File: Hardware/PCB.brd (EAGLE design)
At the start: 46.2 x 35 mm, 105 parts, among them IC1 BQ25180YBGR_BQ25180YBGR, IC2 DRV2605YZFR, IC3 BMA421, IC9 RT6160AWSC, J1 503480-2400, J2 TC2030-IDC_TC2030-IDC, J4 KH-TYPE-C-16P, Q1 20V/4.2A/52mΩ/1.4W, Q3 SI1308EDL-T1-GE3, U1 NRF52840_QF, U3 MAX17048G+T10, X1 32MHz, X2 32.768kHz

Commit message: second commit
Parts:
- moved TP_GND 38.9 mm to (17.9, 97.3)
- moved TP_3.3V 31.8 mm to (21.6, 94.3)
- moved C27 27.9 mm to (19.8, 98.2)
- moved TP_VBAT 27.3 mm to (19.4, 95.3)
- moved D3 26.6 mm to (40.7, 97.4)
- moved TP_SCL 26.4 mm to (19.8, 87.3)
- moved L7 25.6 mm to (25.1, 94.3)
- moved TP_VREG 24.7 mm to (25.6, 91.3)
- moved TP_SWDIO 23.7 mm to (43.7, 93.4)
- moved U3 23.3 mm to (14.7, 97.8)
- moved C6 23.3 mm to (23.1, 77.5), turned to 180 degrees
- moved X2 22.2 mm to (16.8, 81.8)
- moved TP_SDA 22.2 mm to (19.7, 84.3)
- moved C29 22.0 mm to (33.1, 72.2)
- moved TP_SWDCLK 21.3 mm to (39.7, 90.2)
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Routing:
- net SDA/2.4C: track 117.4 -> 23.3 mm, vias 6 -> 4
- net DEC4_6: track 108.0 -> 24.9 mm, vias 10 -> 3
- net 3V3/2.4A: track 184.8 -> 119.8 mm, vias 10 -> 14
- net RESET: track 0.00 -> 34.8 mm, vias 0 -> 2
- net P0.13/1.5D: track 42.2 -> 8.18 mm
- net SCL/1.4C: track 7.60 -> 40.1 mm, vias 0 -> 2
- net SDA/1.4C: track 0.00 -> 31.7 mm, vias 0 -> 2
- net GND: track 399.6 -> 370.7 mm, vias 7 -> 12
- net SWDCLK: track 0.00 -> 26.9 mm, vias 0 -> 2
- net RESE: track 39.1 -> 12.3 mm, vias 5 -> 0
- net EPD_DC: track 0.00 -> 26.0 mm, vias 0 -> 2
- net N$10: track 21.1 -> 1.67 mm, vias 4 -> 0
- net N$13: track 0.00 -> 19.1 mm, vias 0 -> 2
- net N$15: track 9.46 -> 28.3 mm, vias 0 -> 2
- net N$17: track 23.5 -> 4.96 mm, vias 2 -> 0
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- added copper zone on layer 2, net GND

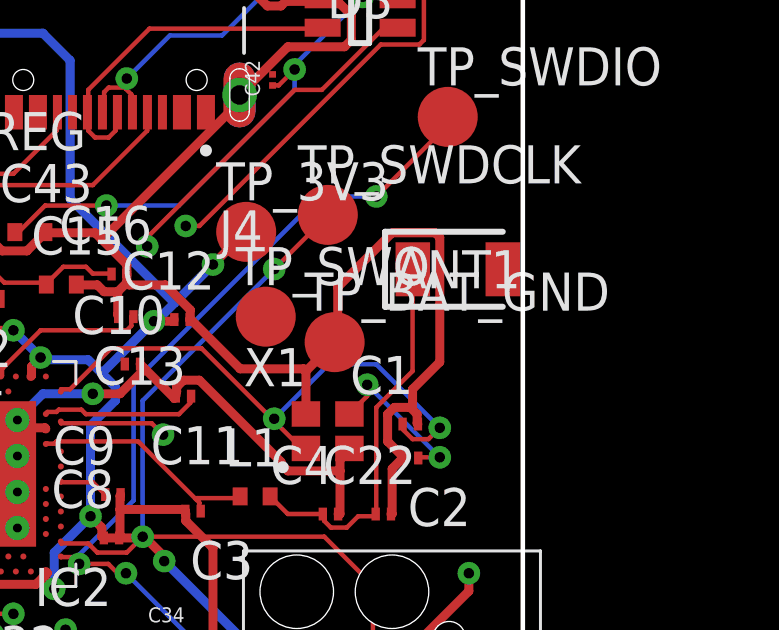
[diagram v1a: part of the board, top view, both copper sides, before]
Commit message: print out schematic
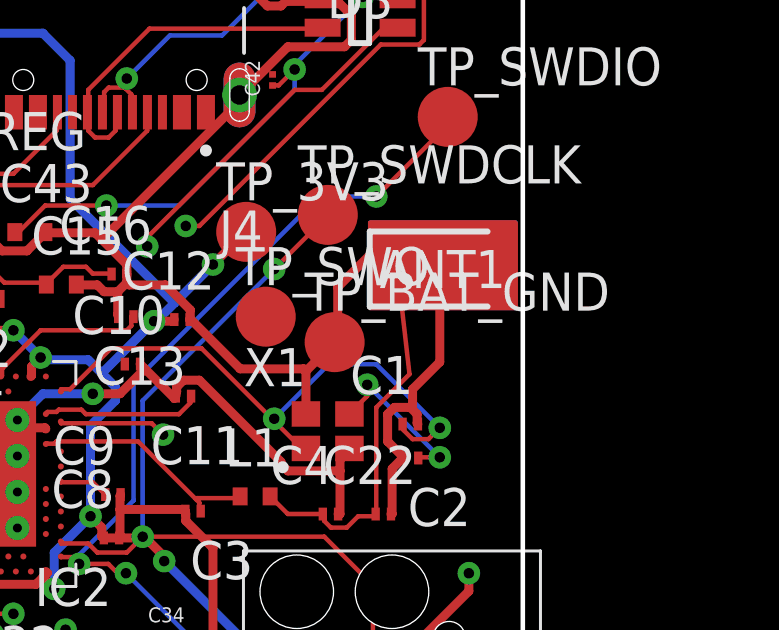
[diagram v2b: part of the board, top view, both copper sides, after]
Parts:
- moved ANT1 0.51 mm to (43.5, 88.4)
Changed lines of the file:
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@@
 <wire x1="38" y1="67" x2="38" y2="65" width="0.1524" layer="20"/>
 <wire x1="38" y1="65" x2="44.162278125" y2="65" width="0.1524" layer="20"/>
+<polygon width="0.1524" layer="2" pour="solid">
+<vertex x="41.0762" y="87.0762"/>
+<vertex x="45.9238" y="87.0762"/>
+<vertex x="45.9238" y="89.9238"/>
+<vertex x="41.0762" y="89.9238"/>
+</polygon>
+<polygon width="0.1524" layer="1" pour="solid">
+<vertex x="41.0762" y="87.0762"/>
+<vertex x="45.9238" y="87.0762"/>
+<vertex x="45.9238" y="89.9238"/>
+<vertex x="41.0762" y="89.9238"/>
+</polygon>
+<polygon width="0.1524" layer="15" pour="solid">
+<vertex x="41.0762" y="87.0762"/>
+<vertex x="45.9238" y="87.0762"/>
+<vertex x="45.9238" y="89.9238"/>
+<vertex x="41.0762" y="89.9238"/>
+</polygon>
+<polygon width="0.1524" layer="16" pour="solid">
+<vertex x="41.0762" y="87.0762"/>
+<vertex x="45.9238" y="87.0762"/>
+<vertex x="45.9238" y="89.9238"/>
+<vertex x="41.0762" y="89.9238"/>
+</polygon>
 </plain>
 <attributes>
@@
 <param name="checkPolygonWidth" value="0"/>
 <param name="useDiameter" value="13"/>
+<param name="flattenRefDes" value="0"/>
 <param name="maxErrors" value="50"/>
 </designrules>
@@
 </autorouter>
 <elements>
-<element name="ANT1" library="InkTime_v5" package="2450AT18B100E_ANTC3216X140N" value="2450AT18B100E_2450AT18B100E" x="43.99508125" y="88.37" smashed="yes">
-<attribute name="ARROW_PART_NUMBER" value="2450AT18B100E" x="145.59508125" y="-78" size="1.778" layer="27" display="off"/>
-<attribute name="ARROW_PRICE-STOCK" value="https://www.arrow.com/en/products/2450at18b100e/johanson-dielectrics?utm_currency=USD&amp;region=nac" x="145.59508125" y="-78" size="1.778" layer="27" display="off"/>
-<attribute name="DESCRIPTION" value="Antennas 2.45GHz ANTENNA" x="145.59508125" y="-78" size="1.778" layer="27" display="off"/>
-<attribute name="HEIGHT" value="1.4mm" x="145.59508125" y="-78" size="1.778" layer="27" display="off"/>
-<attribute name="MANUFACTURER_NAME" value="JOHANSON TECHNOLOGY" x="145.59508125" y="-78" size="1.778" layer="27" display="off"/>
-<attribute name="MANUFACTURER_PART_NUMBER" value="2450AT18B100E" x="145.59508125" y="-78" size="1.778" layer="27" display="off"/>
-<attribute name="MOUSER_PART_NUMBER" value="609-2450AT18B100E" x="145.59508125" y="-78" size="1.778" layer="27" display="off"/>
-<attribute name="MOUSER_PRICE-STOCK" value="https://www.mouser.co.uk/ProductDetail/Johanson-Technology/2450AT18B100E?qs=yCnrNFeXz%252Bh5MFsFIXGZGA%3D%3D" x="145.59508125" y="-78" size="1.778" layer="27" display="off"/>
-<attribute name="NAME" x="43.99508125" y="88.37" size="1.27" layer="25" align="center"/>
-<attribute name="VALUE" x="43.99508125" y="88.37" size="1.27" layer="27" align="center"/>
+<element name="ANT1" library="InkTime_v5" package="2450AT18B100E_ANTC3216X140N" value="2450AT18B100E_2450AT18B100E" x="43.485721875" y="88.37668125" smashed="yes">
+<attribute name="ARROW_PART_NUMBER" value="2450AT18B100E" x="145.085721875" y="-77.99331875" size="1.778" layer="27" display="off"/>
+<attribute name="ARROW_PRICE-STOCK" value="https://www.arrow.com/en/products/2450at18b100e/johanson-dielectrics?utm_currency=USD&amp;region=nac" x="145.085721875" y="-77.99331875" size="1.778" layer="27" display="off"/>
+<attribute name="DESCRIPTION" value="Antennas 2.45GHz ANTENNA" x="145.085721875" y="-77.99331875" size="1.778" layer="27" display="off"/>
+<attribute name="HEIGHT" value="1.4mm" x="145.085721875" y="-77.99331875" size="1.778" layer="27" display="off"/>
+<attribute name="MANUFACTURER_NAME" value="JOHANSON TECHNOLOGY" x="145.085721875" y="-77.99331875" size="1.778" layer="27" display="off"/>
+<attribute name="MANUFACTURER_PART_NUMBER" value="2450AT18B100E" x="145.085721875" y="-77.99331875" size="1.778" layer="27" display="off"/>
+<attribute name="MOUSER_PART_NUMBER" value="609-2450AT18B100E" x="145.085721875" y="-77.99331875" size="1.778" layer="27" display="off"/>
+<attribute name="MOUSER_PRICE-STOCK" value="https://www.mouser.co.uk/ProductDetail/Johanson-Technology/2450AT18B100E?qs=yCnrNFeXz%252Bh5MFsFIXGZGA%3D%3D" x="145.085721875" y="-77.99331875" size="1.778" layer="27" display="off"/>
+<attribute name="NAME" x="43.485721875" y="88.37668125" size="1.27" layer="25" align="center"/>
+<attribute name="VALUE" x="43.485721875" y="88.37668125" size="1.27" layer="27" align="center"/>
 </element>
 <element name="C1" library="InkTime_v5" package="NORDIC_NRF_3_RESC0201_L" value="12pF" x="42.41" y="83.21" smashed="yes">
@@
 <wire x1="41.202" y1="80.136" x2="41.2576" y2="80.21" width="0.15" layer="1"/>
 <wire x1="39.5388" y1="80.136" x2="39.495" y2="80.21" width="0.15" layer="1"/>
-<wire x1="42.4872" y1="84.9744" x2="42.4872" y2="88.3008" width="0.15" layer="1"/>
-<wire x1="41.2776" y1="83.7648" x2="42.4872" y2="84.9744" width="0.15" layer="1"/>
+<wire x1="41.2776" y1="83.7648" x2="42.384865625" y2="84.872065625" width="0.15" layer="1"/>
 <wire x1="41.2776" y1="80.2872" x2="41.2776" y2="83.7648" width="0.15" layer="1"/>
-<wire x1="42.4872" y1="88.3008" x2="42.49508125" y2="88.37" width="0.15" layer="1"/>
+<wire x1="42.384865625" y1="84.872065625" x2="41.985721875" y2="88.37668125" width="0.15" layer="1"/>
 <wire x1="41.2776" y1="80.2872" x2="41.2576" y2="80.21" width="0.15" layer="1"/>
 </signal>
@@
 <wire x1="30.618" y1="93.5928" x2="30.65" y2="93.6038" width="0.15" layer="1"/>
 </signal>
+<signal name="N$2">
+</signal>
 </signals>
